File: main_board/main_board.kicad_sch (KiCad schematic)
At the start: 11 parts, among them U2 TS5A4624DCKR, U4 TS5A4624DCKR

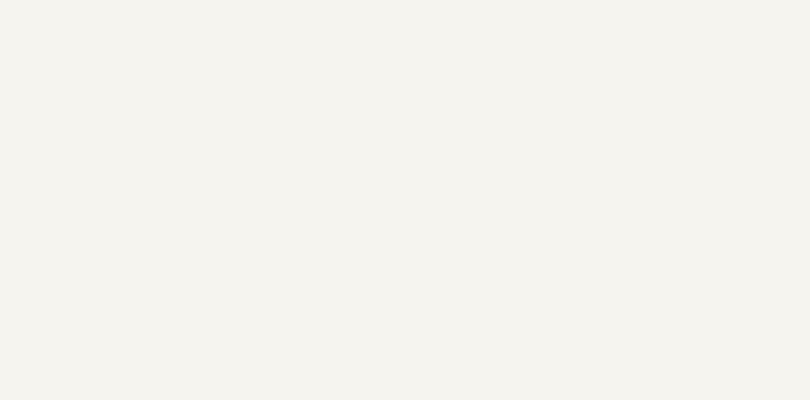
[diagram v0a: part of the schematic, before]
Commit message: added step down converter circuit to convert 9v to 5v at 2 A.
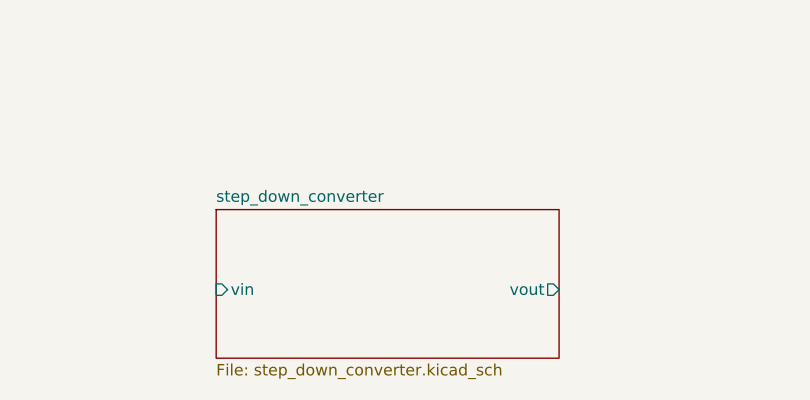
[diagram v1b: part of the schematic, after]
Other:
- added sheet step_down_converter (step_down_converter.kicad_sch)
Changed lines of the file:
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@@
+	)
+	(sheet
+		(at 175.26 129.54)
+		(size 38.1 16.51)
+		(exclude_from_sim no)
+		(in_bom yes)
+		(on_board yes)
+		(dnp no)
+		(fields_autoplaced yes)
+		(stroke
+			(width 0.1524)
+			(type solid)
+		)
+		(fill
+			(color 0 0 0 0.0000)
+		)
+		(property "Sheetname" "step_down_converter"
+			(at 175.26 128.8284 0)
+			(effects
+				(font
+					(size 1.27 1.27)
+				)
+				(justify left bottom)
+			)
+		)
+		(property "Sheetfile" "step_down_converter.kicad_sch"
+			(at 175.26 146.6346 0)
+			(effects
+				(font
+					(size 1.27 1.27)
+				)
+				(justify left top)
+			)
+		)
+		(pin "vin" input
+			(at 175.26 138.43 180)
+			(effects
+				(font
+					(size 1.27 1.27)
+				)
+				(justify left)
+			)
+		)
+		(pin "vout" output
+			(at 213.36 138.43 0)
+			(effects
+				(font
+					(size 1.27 1.27)
+				)
+				(justify right)
+			)
+		)
+		(instances
+			(project "main_board"
+				(path "/f3e20914-54f5-4568-9f0b-8875d87df3fb"
+					(page "6")
+				)
+			)
+		)
 	)
 	(sheet

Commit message: tweaks
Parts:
- added U10: ~, Cmod_S7:Cmod_S7, symbol Cmod_S7:Cmod_S7

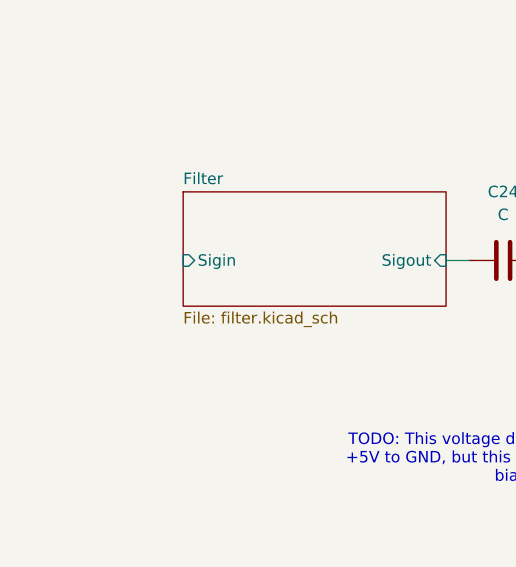
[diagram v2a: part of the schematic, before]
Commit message: biasing for driver to adc.
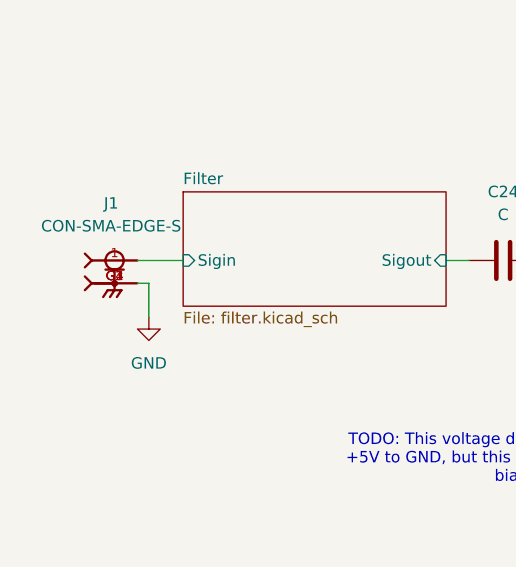
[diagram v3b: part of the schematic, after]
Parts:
- added J1: CON-SMA-EDGE-S, CON-SMA-EDGE-S:RFSOLUTIONS_CON-SMA-EDGE-S, symbol SMA_MALE_connector:CON-SMA-EDGE-S
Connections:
- net Filter/Sigin: now also J1.1
- net GND: now also J1.G1, J1.G2, J1.G3, J1.G4
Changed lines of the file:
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@@
+	(wire
+		(pts
+			(xy 19.05 83.82) (xy 20.32 83.82)
+		)
+		(stroke
+			(width 0)
+			(type default)
+		)
+	)
 	(wire
 		(pts
@@
 	(wire
 		(pts
+			(xy 19.05 81.28) (xy 24.13 81.28)
+		)
+		(stroke
+			(width 0)
+			(type default)
+		)
+	)
+	(wire
+		(pts
 			(xy 66.04 77.47) (xy 66.04 81.28)
 		)
@@
 		(pts
 			(xy 257.81 26.67) (xy 269.24 26.67)
+		)
+		(stroke
+			(width 0)
+			(type default)
+		)
+	)
+	(wire
+		(pts
+			(xy 20.32 83.82) (xy 20.32 87.63)
 		)
 		(stroke
@@
 	)
 	(symbol
+		(lib_id "power:GND")
+		(at 20.32 87.63 0)
+		(unit 1)
+		(exclude_from_sim no)
+		(in_bom yes)
+		(on_board yes)
+		(dnp no)
+		(fields_autoplaced yes)
+		(property "Reference" "#PWR043"
+			(at 20.32 93.98 0)
+			(effects
+				(font
+					(size 1.27 1.27)
+				)
+				(hide yes)
+			)
+		)
+		(property "Value" "GND"
+			(at 20.32 92.71 0)
+			(effects
+				(font
+					(size 1.27 1.27)
+				)
+			)
+		)
+		(property "Footprint" ""
+			(at 20.32 87.63 0)
+			(effects
+				(font
+					(size 1.27 1.27)
+				)
+				(hide yes)
+			)
+		)
+		(property "Datasheet" ""
+			(at 20.32 87.63 0)
+			(effects
+				(font
+					(size 1.27 1.27)
+				)
+				(hide yes)
+			)
+		)
+		(property "Description" "Power symbol creates a global label with name \"GND\" , ground"
+			(at 20.32 87.63 0)
+			(effects
+				(font
+					(size 1.27 1.27)
+				)
+				(hide yes)
+			)
+		)
+		(pin "1"
+		)
+		(instances
+			(project ""
+				(path "/f3e20914-54f5-4568-9f0b-8875d87df3fb"
+					(reference "#PWR043")
+					(unit 1)
+				)
+			)
+		)
+	)
+	(symbol
 		(lib_id "Cmod_S7:Cmod_S7")
 		(at 124.46 139.7 0)
@@
 					(unit 1)
 				)
+			)
+		)
+	)
+	(symbol
+		(lib_id "SMA_MALE_connector:CON-SMA-EDGE-S")
+		(at 16.51 83.82 0)
+		(unit 1)
+		(exclude_from_sim no)
+		(in_bom yes)
+		(on_board yes)
+		(dnp no)
+		(fields_autoplaced yes)
+		(property "Reference" "J1"
+			(at 16.129 74.93 0)
+			(effects
+				(font
+					(size 1.27 1.27)
+				)
+			)
+		)
+		(property "Value" "CON-SMA-EDGE-S"
+			(at 16.129 77.47 0)
+			(effects
+				(font
+					(size 1.27 1.27)
+				)
+			)
+		)
+		(property "Footprint" "CON-SMA-EDGE-S:RFSOLUTIONS_CON-SMA-EDGE-S"
+			(at 16.51 83.82 0)
+			(effects
+				(font
+					(size 1.27 1.27)
+				)
+				(justify bottom)
+				(hide yes)
+			)
+		)
+		(property "Datasheet" ""
+			(at 16.51 83.82 0)
+			(effects
+				(font
+					(size 1.27 1.27)
+				)
+				(hide yes)
+			)
+		)
+		(property "Description" ""
+			(at 16.51 83.82 0)
+			(effects
+				(font
+					(size 1.27 1.27)
+				)
+				(hide yes)
+			)
+		)
+		(property "PARTREV" "1"
+			(at 16.51 83.82 0)
+			(effects
+				(font
+					(size 1.27 1.27)
+				)
+				(justify bottom)
+				(hide yes)
+			)
+		)
+		(property "STANDARD" "Manufacturer Recommendations"
+			(at 16.51 83.82 0)
+			(effects
+				(font
+					(size 1.27 1.27)
+				)
+				(justify bottom)
+				(hide yes)
+			)
+		)
+		(property "MAXIMUM_PACKAGE_HEIGHT" "6.35mm"
+			(at 16.51 83.82 0)
+			(effects
+				(font
+					(size 1.27 1.27)
+				)
+				(justify bottom)
+				(hide yes)
+			)
+		)
+		(property "MANUFACTURER" "RF Solutions"
+			(at 16.51 83.82 0)
+			(effects
+				(font
+					(size 1.27 1.27)
+				)
+				(justify bottom)
+				(hide yes)
+			)
+		)
+		(pin "G4"
+		)
+		(pin "G3"
+		)
+		(pin "1"
+		)
+		(pin "G1"
+		)
+		(pin "G2"
+		)
+		(instances
+			(project ""
+				(path "/f3e20914-54f5-4568-9f0b-8875d87df3fb"
+					(reference "J1")
+					(unit 1)
+				)

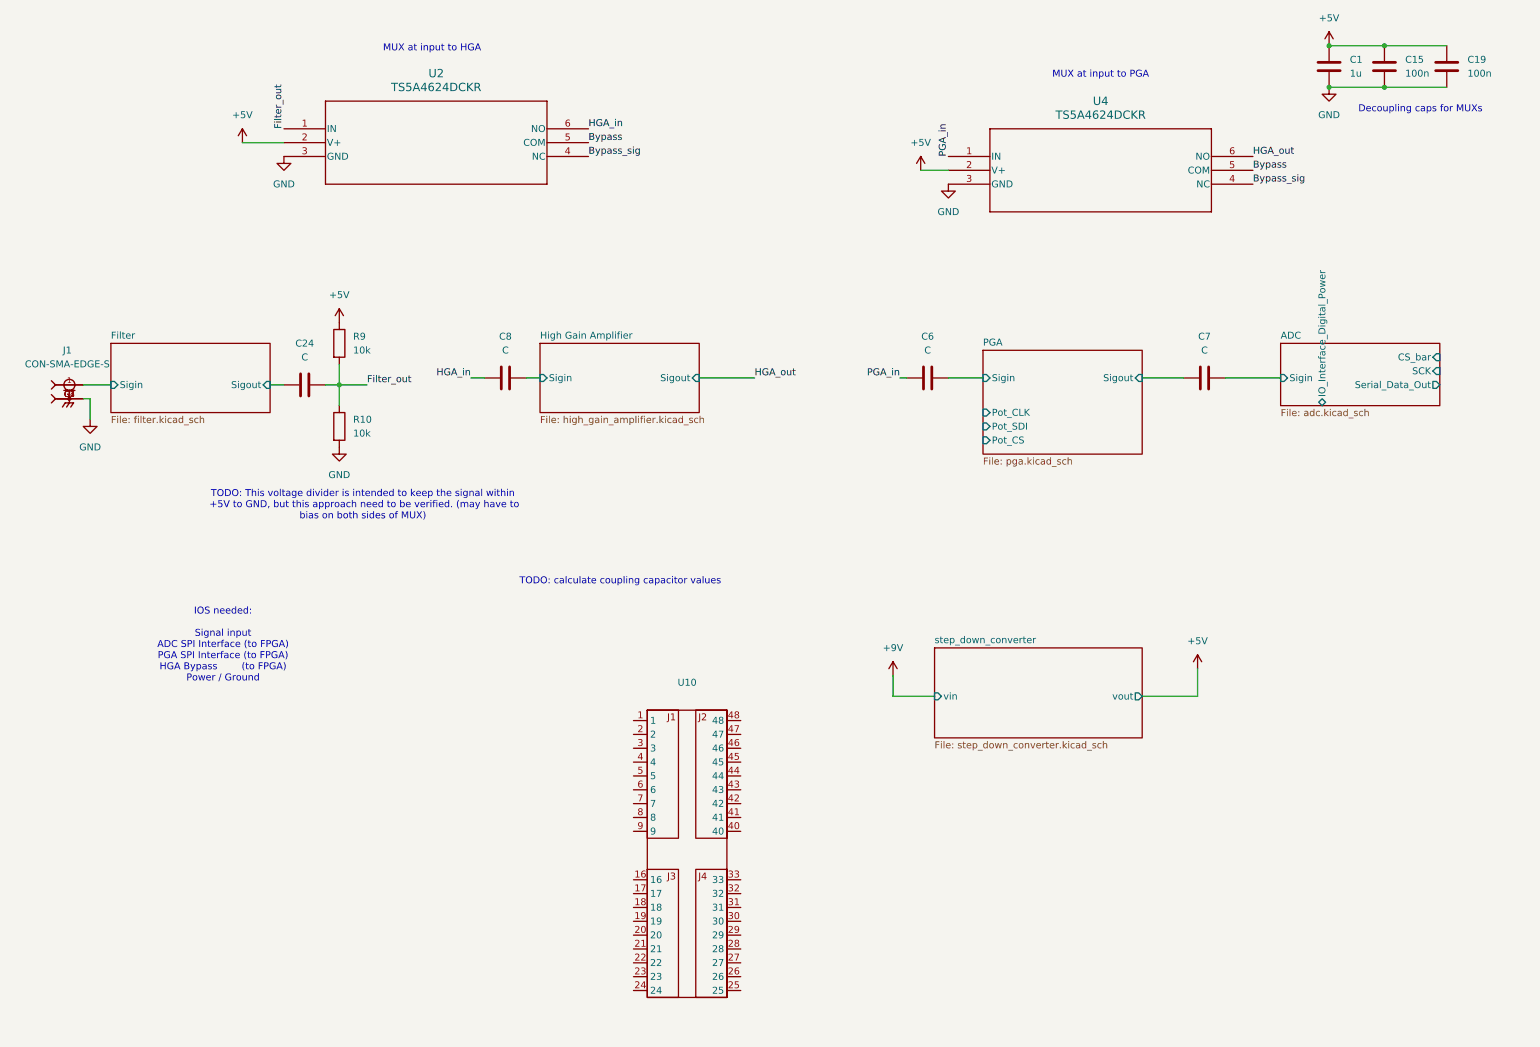
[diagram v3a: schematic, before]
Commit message: added linear voltage regulator.
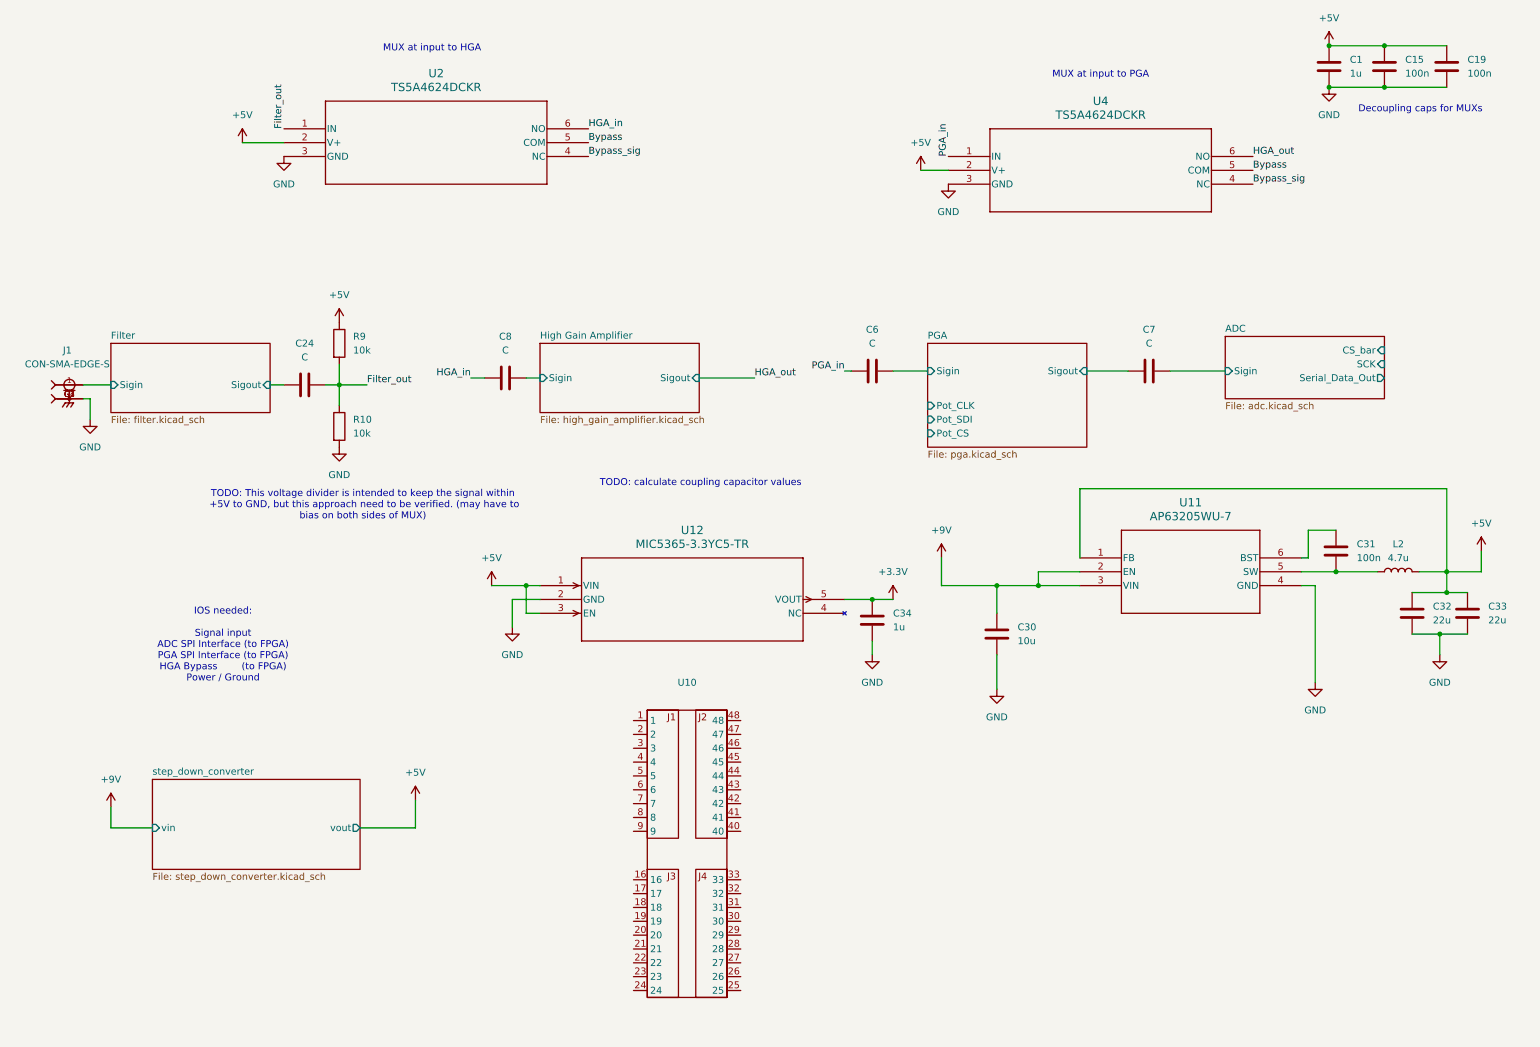
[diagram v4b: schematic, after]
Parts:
- added C30: 10u, symbol Device:C
- added C31: 100n, symbol Device:C
- added C32, C33: 22u, symbol Device:C
- added C34: 1u, symbol Device:C
- added L2: 4.7u, symbol Device:L
- added U11: AP63205WU-7, SOIC_05WU-7_DIO, symbol step_down_converter:AP63205WU-7
- added U12: MIC5365-3.3YC5-TR, SC-70_C5_MCH, symbol linear_regulartor:MIC5365-3.3YC5-TR
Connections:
- net +5V: now also C32.1, C33.1, L2.2, U11.1 (FB), U12.1 (VIN), U12.3 (EN)
- net +9V: now also C30.1, U11.2 (EN), U11.3 (VIN)
- net GND: now also C30.2, C32.2, C33.2, C34.2, U11.4 (GND), U12.2 (GND)
- new net: C31.1, U11.6 (BST)
- new net: C31.2, L2.1, U11.5 (SW)
- new net +3.3V: C34.1, U12.5 (VOUT)
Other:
- sheet ADC ports: added none; removed IO_Interface_Digital_Power
- moved on the sheet: C6, C7

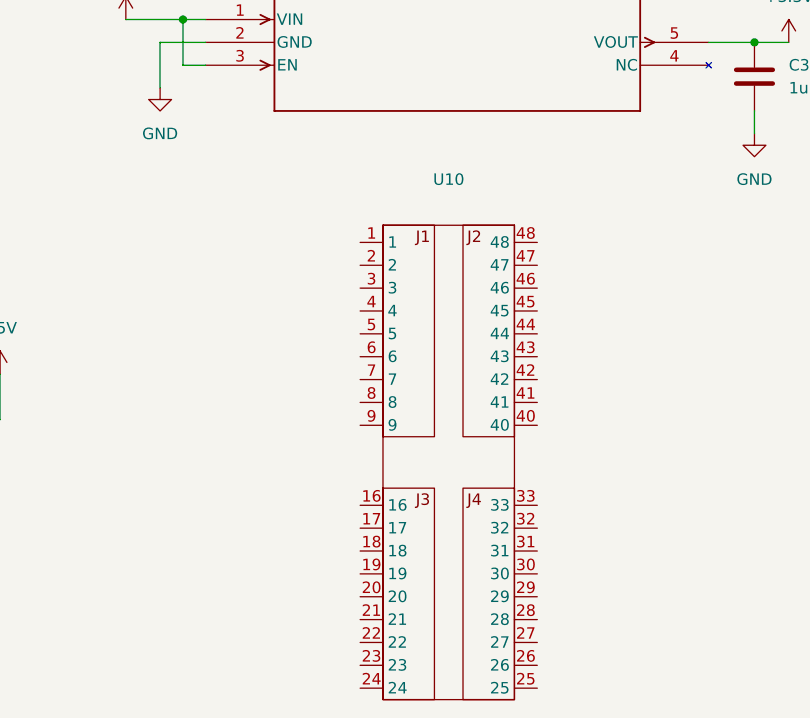
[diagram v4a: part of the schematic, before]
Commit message: readd fpga power
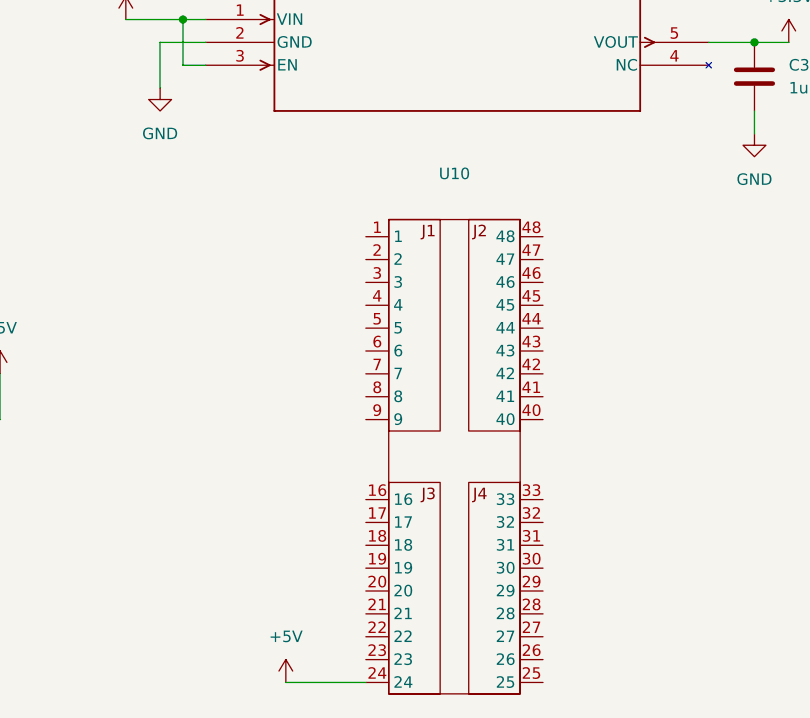
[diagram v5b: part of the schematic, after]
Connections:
- net +5V: now also U10.24
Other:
- moved on the sheet: U10
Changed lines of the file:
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@@
+	(wire
+		(pts
+			(xy 111.76 191.77) (xy 120.65 191.77)
+		)
+		(stroke
+			(width 0)
+			(type default)
+		)
+	)
 	(wire
 		(pts
@@
 	(symbol
 		(lib_id "Cmod_S7:Cmod_S7")
-		(at 124.46 139.7 0)
+		(at 125.095 139.065 0)
 		(unit 1)
 		(exclude_from_sim no)
@@
 		(fields_autoplaced yes)
 		(property "Reference" "U10"
-			(at 129.8575 135.89 0)
+			(at 130.4925 135.255 0)
 			(effects
 				(font
@@
 		)
 		(property "Value" "~"
-			(at 129.8575 138.43 0)
+			(at 130.4925 137.795 0)
 			(effects
 				(font
@@
 		)
 		(property "Footprint" "Cmod_S7:Cmod_S7"
-			(at 124.46 139.7 0)
+			(at 125.095 139.065 0)
 			(effects
 				(font
@@
 		)
 		(property "Datasheet" ""
-			(at 124.46 139.7 0)
+			(at 125.095 139.065 0)
 			(effects
 				(font
@@
 		)
 		(property "Description" ""
-			(at 124.46 139.7 0)
+			(at 125.095 139.065 0)
 			(effects
 				(font
@@
 					(unit 1)
 				)
+			)
+		)
+	)
+	(symbol
+		(lib_id "power:+5V")
+		(at 111.76 191.77 0)
+		(unit 1)
+		(exclude_from_sim no)
+		(in_bom yes)
+		(on_board yes)
+		(dnp no)
+		(fields_autoplaced yes)
+		(property "Reference" "#PWR055"
+			(at 111.76 195.58 0)
+			(effects
+				(font
+					(size 1.27 1.27)
+				)
+				(hide yes)
+			)
+		)
+		(property "Value" "+5V"
+			(at 111.76 186.69 0)
+			(effects
+				(font
+					(size 1.27 1.27)
+				)
+			)
+		)
+		(property "Footprint" ""
+			(at 111.76 191.77 0)
+			(effects
+				(font
+					(size 1.27 1.27)
+				)
+				(hide yes)
+			)
+		)
+		(property "Datasheet" ""
+			(at 111.76 191.77 0)
+			(effects
+				(font
+					(size 1.27 1.27)
+				)
+				(hide yes)
+			)
+		)
+		(property "Description" "Power symbol creates a global label with name \"+5V\""
+			(at 111.76 191.77 0)
+			(effects
+				(font
+					(size 1.27 1.27)
+				)
+				(hide yes)
+			)
+		)
+		(pin "1"
+		)
+		(instances
+			(project ""
+				(path "/f3e20914-54f5-4568-9f0b-8875d87df3fb"
+					(reference "#PWR055")
+					(unit 1)
+				)

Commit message: reorganize
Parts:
- removed C30: 10u, symbol Device:C
- removed C31: 100n, symbol Device:C
- removed C32, C33: 22u, symbol Device:C
- removed C34: 1u, symbol Device:C
- removed L2: 4.7u, symbol Device:L
- removed U11: AP63205WU-7, SOIC_05WU-7_DIO, symbol step_down_converter:AP63205WU-7
- removed U12: MIC5365-3.3YC5-TR, SC-70_C5_MCH, symbol linear_regulartor:MIC5365-3.3YC5-TR
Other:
- sheet step_down_converter renamed power
- sheet power: file step_down_converter.kicad_sch -> power.kicad_sch
